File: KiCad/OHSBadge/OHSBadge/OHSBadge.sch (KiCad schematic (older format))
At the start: 100 parts, among them J4 ZIF-40-0.5, P1 PCB, P2 ISP, P3 FTDI, P4 C3SB, P5 JST_3V7, P6 V_IN, P7 UUSB_B, Q1 DMG2301U-7, Q2 2N7002KW, Q3 BSS84W, Q4 2N7002KW, Q5 2N7002KW, Q6 2N7002KW, Q7 BSS84W, SW1 UP, SW2 SEL, SW3 DOWN, SW4 RST, SW5 MODE, U1 MCP9700AT-E/TT, U2 ATMEGA328-AU-ND, U3 MCP1700T-33, U4 TXS0108, U5 DS1307, U5/7 I/O, U6 MCP1702T-50, X1 8MHz, X2 32.768kHz

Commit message: BADGEr v3 swap LED and TEMP.
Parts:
- added G5: OSHW, OSHW_logo, symbol PCB
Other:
- note added: "NOTE : S_LINK (SL1) is bridged [ D2 is bypassed ] when powering the Badge\nfrom the Coin Battery.\nWhen using ANY OTHER power source (Lipo on JST, 5V on USB, 12V Barrel\nsocket etc), Unbridge D2 (remove solder from link SL1).\nThe Coin Battery can then be used as power source for RTC.\nIf RTC is not used, REMOVE the Coin Battery."
- note added: "see NOTE"
- moved on the sheet: H5, H6
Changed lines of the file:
@@
-EESchema Schematic File Version 2  date 23-May-13 1:45:22 PM
+EESchema Schematic File Version 2
 LIBS:OHSBadge_sym
 LIBS:OHSBadge-cache
-EELAYER 27 0
+EELAYER 24 0
 EELAYER END
 $Descr A4 11693 8268
@@
 Text Label 6150 6750 0    40   ~ 0
 SPI_SS_3V3
-Text Label 6150 4750 0    40   ~ 0
+Text Label 6150 5450 0    40   ~ 0
 TEMPERATURE
 Text Label 2025 4275 0    30   ~ 0
@@
 Text Label 6150 5350 0    40   ~ 0
 MODE
-Text Label 6150 5450 0    40   ~ 0
+Text Label 6150 4750 0    40   ~ 0
 AD7_3V3
 Text Label 3825 4100 0    40   ~ 0
@@
 L I/O H5
 U 1 1 5170D6BA
-P 2150 7525
-F 0 "H5" V 2225 7475 40  0000 L CNN
-F 1 "I/O" H 2150 7580 30  0001 C CNN
-F 2 "vite_3mm" H 2150 7525 60  0001 C CNN
-F 3 "~" H 2150 7525 60  0000 C CNN
-	1    2150 7525
+P 2550 7525
+F 0 "H5" V 2625 7475 40  0000 L CNN
+F 1 "I/O" H 2550 7580 30  0001 C CNN
+F 2 "vite_3mm" H 2550 7525 60  0001 C CNN
+F 3 "~" H 2550 7525 60  0000 C CNN
+	1    2550 7525
 	0    -1   -1   0
 $EndComp
@@
 L I/O H6
 U 1 1 5170D6F4
-P 2350 7525
-F 0 "H6" V 2425 7475 40  0000 L CNN
-F 1 "I/O" H 2350 7580 30  0001 C CNN
-F 2 "vite_3mm" H 2350 7525 60  0001 C CNN
-F 3 "~" H 2350 7525 60  0000 C CNN
-	1    2350 7525
+P 2750 7525
+F 0 "H6" V 2825 7475 40  0000 L CNN
+F 1 "I/O" H 2750 7580 30  0001 C CNN
+F 2 "vite_3mm" H 2750 7525 60  0001 C CNN
+F 3 "~" H 2750 7525 60  0000 C CNN
+	1    2750 7525
 	0    -1   -1   0
 $EndComp
-NoConn ~ 2350 7675
-NoConn ~ 2150 7675
+NoConn ~ 2750 7675
+NoConn ~ 2550 7675
 $Comp
 L S_LINK SL1
 U 1 1 5170DF18
 P 10750 6150
-F 0 "SL1" H 10850 6100 30  0000 C CNN
-F 1 "S_LINK" H 10900 6150 30  0000 C CNN
+F 0 "SL1" H 10875 6175 30  0000 C CNN
+F 1 "S_LINK" H 10900 6225 30  0000 C CNN
 F 2 "ShortLink" H 10750 6150 60  0001 C CNN
 F 3 "" H 10750 6150 60  0000 C CNN
@@
 Text Label 6150 5850 0    40   ~ 0
 UP
+Text Notes 8325 5275 0    30   ~ 0
+NOTE : S_LINK (SL1) is bridged [ D2 is bypassed ] when powering the Badge\nfrom the Coin Battery.\nWhen using ANY OTHER power source (Lipo on JST, 5V on USB, 12V Barrel\nsocket etc), Unbridge D2 (remove solder from link SL1).\nThe Coin Battery can then be used as power source for RTC.\nIf RTC is not used,  REMOVE the Coin Battery.
+Text Notes 10825 6200 0    30   ~ 0
+see NOTE
+Wire Notes Line
+	8300 5200 10150 5200
+Wire Notes Line
+	10150 5200 10150 5550
+Wire Notes Line
+	10150 5550 8300 5550
+Wire Notes Line
+	8300 5550 8300 5200
+$Comp
+L PCB G5
+U 1 1 51AE0BF3
+P 2200 7600
+F 0 "G5" H 2200 7550 40  0000 C CNN
+F 1 "OSHW" H 2200 7650 40  0000 C CNN
+F 2 "OSHW_logo" H 2200 7600 60  0001 C CNN
+F 3 "" H 2200 7600 60  0000 C CNN
+	1    2200 7600
+	1    0    0    -1
+$EndComp
 $EndSCHEMATC

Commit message: OHSBadge : BADGEr_v3 Final Prototype. Added PDF Files. Minor mods.
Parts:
- D3: footprint (none) -> led_0805
- G5: footprint OSHW_logo -> OHS2013
- J4: footprint ZIF-40-0.5-M_Hirose -> ZIF-40-0.5-M_seeed
- SD1: footprint SD_Micro -> SD_Micro_seeed
- U4: footprint SO20L -> TXS0108EPWR
- renumbered AD7 to A0, AD7_3V3 to A0_3V3, A3 to XA3, B3 to XB3
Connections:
- net labels added: A0, A0_3V3
- net labels removed: AD7, AD7_3V3
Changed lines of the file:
@@
-EESchema Schematic File Version 2
+EESchema Schematic File Version 2  date 05-Jun-13 3:48:10 PM
 LIBS:OHSBadge_sym
 LIBS:OHSBadge-cache
-EELAYER 24 0
+EELAYER 27 0
 EELAYER END
 $Descr A4 11693 8268
@@
 Sheet 1 1
 Title ""
-Date "23 may 2013"
+Date "5 jun 2013"
 Rev ""
 Comp ""
@@
 F 0 "J4" H 11075 300 27  0000 L TNN
 F 1 "ZIF-40-0.5" H 10875 -1475 27  0000 L TNN
-F 2 "ZIF-40-0.5-M_Hirose" H 10500 575 27  0001 L TNN
+F 2 "ZIF-40-0.5-M_seeed" H 10500 575 27  0001 L TNN
 F 3 "" H 10450 525 60  0001 C CNN
 	1    10450 525
@@
 F 0 "U4" H 1525 3775 40  0000 C CNN
 F 1 "TXS0108" H 1525 3875 40  0000 C CNN
-F 2 "SO20L" H 1525 4175 60  0001 C CNN
+F 2 "TXS0108EPWR" H 1525 4175 60  0001 C CNN
 F 3 "" H 1525 4175 60  0000 C CNN
 	1    1525 4175
@@
 F 0 "SD1" H 1950 3325 40  0000 C CNN
 F 1 "SD_CARD_MICRO" H 2375 3325 40  0000 C CNN
-F 2 "SD_Micro" H 1800 2875 60  0001 C CNN
+F 2 "SD_Micro_seeed" H 1800 2875 60  0001 C CNN
 F 3 "" H 1800 2875 60  0001 C CNN
 	1    1800 2875
@@
 MODE
 Text Label 6150 4750 0    40   ~ 0
-AD7_3V3
+A0_3V3
 Text Label 3825 4100 0    40   ~ 0
 3V3
@@
 $EndComp
 $Comp
-L I/O AD7_3V3
+L I/O A0_3V3
 U 1 1 5159E685
 P 2175 4075
-F 0 "AD7_3V3" H 2225 4075 40  0000 L CNN
+F 0 "A0_3V3" H 2225 4075 40  0000 L CNN
 F 1 "I/O" H 2175 4020 30  0001 C CNN
 F 2 "I/O" H 2175 4075 60  0001 C CNN
@@
 Text Label 3775 1850 0    40   ~ 0
 GND
-Text Label 3775 1750 0    40   ~ 0
-SH_5V
 Text Label 3775 1450 0    40   ~ 0
 SH_5V
@@
 $EndComp
 Text Label 1925 4075 0    30   ~ 0
-AD7_3V3
+A0_3V3
 Text Label 2025 3975 0    30   ~ 0
 SPI_SS_3V3
 Text Label 925  4075 0    30   ~ 0
-AD7
+A0
 Text Label 925  3975 0    30   ~ 0
 SPI_SS
 $Comp
-L I/O AD7
+L I/O A0
 U 1 1 51627367
 P 775 4075
-F 0 "AD7" H 825 4075 40  0000 L CNN
+F 0 "A0" H 825 4075 40  0000 L CNN
 F 1 "I/O" H 775 4020 30  0001 C CNN
 F 2 "I/O" H 775 4075 60  0001 C CNN
@@
 $EndComp
 $Comp
-L I/O B3
+L I/O XB3
 U 1 1 5162736D
 P 775 4175
-F 0 "B3" H 855 4175 40  0000 L CNN
+F 0 "XB3" H 825 4175 40  0000 L CNN
 F 1 "I/O" H 775 4120 30  0001 C CNN
 F 2 "I/O" H 775 4175 60  0001 C CNN
@@
 	3775 1850 4025 1850
 Wire Wire Line
-	3775 1750 4025 1750
-Wire Wire Line
-	3575 1450 4025 1450
-Wire Wire Line
 	8425 6475 8425 6575
 Connection ~ 8425 6000
@@
 Connection ~ 6775 5350
 $Comp
-L I/O A3
+L I/O XA3
 U 1 1 51645932
 P 2175 4175
-F 0 "A3" H 2255 4175 40  0000 L CNN
+F 0 "XA3" H 2225 4175 40  0000 L CNN
 F 1 "I/O" H 2175 4120 30  0001 C CNN
 F 2 "I/O" H 2175 4175 60  0001 C CNN
@@
 Text Label 7950 6000 0    30   ~ 0
 V_IN
-$Comp
-L PWR_FLAG #FLG027
-U 1 1 51669725
-P 3575 1400
-F 0 "#FLG027" H 3575 1305 30  0001 C CNN
-F 1 "PWR_FLAG" V 3475 1500 30  0000 C CNN
-F 2 "" H 3575 1400 60  0000 C CNN
-F 3 "" H 3575 1400 60  0000 C CNN
-	1    3575 1400
-	1    0    0    -1
-$EndComp
-Wire Wire Line
-	3575 1450 3575 1400
 $Comp
 L UUSB_B P7
@@
 	2575 4925 2575 4075
 $Comp
-L PWR_FLAG #FLG028
+L PWR_FLAG #FLG027
 U 1 1 516131E6
 P 10900 5925
-F 0 "#FLG028" H 10900 5830 30  0001 C CNN
+F 0 "#FLG027" H 10900 5830 30  0001 C CNN
 F 1 "PWR_FLAG" H 10900 6100 30  0000 C CNN
 F 2 "" H 10900 5925 60  0000 C CNN
@@
 F 0 "D3" V 10925 4950 30  0000 C CNN
 F 1 "DEBUG" V 10875 5000 30  0000 C CNN
-F 2 "" H 10925 5175 60  0000 C CNN
+F 2 "led_0805" H 10925 5175 60  0001 C CNN
 F 3 "~" H 10925 5175 60  0000 C CNN
 	1    10925 5175
@@
 	10925 5375 10925 5475
 $Comp
-L GND #PWR029
+L GND #PWR028
 U 1 1 519C90C8
 P 10925 5475
-F 0 "#PWR029" H 10925 5475 30  0001 C CNN
+F 0 "#PWR028" H 10925 5475 30  0001 C CNN
 F 1 "GND" H 10925 5545 30  0001 C CNN
 F 2 "" H 10925 5475 60  0000 C CNN
@@
 	10925 4600 10475 4600
 Text Label 10475 4600 0    40   ~ 0
-AD7_3V3
+A0_3V3
 Wire Notes Line
 	10325 4475 11175 4475
@@
 F 0 "G5" H 2200 7550 40  0000 C CNN
 F 1 "OSHW" H 2200 7650 40  0000 C CNN
-F 2 "OSHW_logo" H 2200 7600 60  0001 C CNN
+F 2 "OHS2013" H 2200 7600 60  0001 C CNN
 F 3 "" H 2200 7600 60  0000 C CNN
 	1    2200 7600
 	1    0    0    -1
 $EndComp
+Wire Wire Line
+	4025 1450 3700 1450
+Wire Wire Line
+	3700 1450 3700 1750
+Wire Wire Line
+	3700 1750 4025 1750
 $EndSCHEMATC

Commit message: OHSBadge : BADGEr_v3 Final Prototype. push buttons changed to SMD. Added SMD ON switch for BATTERY. Centered P-Buttons with EPD.
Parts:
- added SW6: SW_ON, SW_SLIDE_seeed, symbol SW_SLIDE
- SW1, SW2, SW3, SW4, SW5: footprint SW-PB -> SW_SMD
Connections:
- net labels added: BATT
- wire segments 368 -> 372
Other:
- moved on the sheet: D3, R14
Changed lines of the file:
@@
-EESchema Schematic File Version 2  date 05-Jun-13 3:48:10 PM
+EESchema Schematic File Version 2  date 07-Jun-13 5:07:04 PM
 LIBS:OHSBadge_sym
 LIBS:OHSBadge-cache
@@
 Sheet 1 1
 Title ""
-Date "5 jun 2013"
+Date "7 jun 2013"
 Rev ""
 Comp ""
@@
 Text Label 875  1725 0    24   ~ 0
 3V3
-Text Label 10600 6000 0    30   ~ 0
+Text Label 10900 6000 0    30   ~ 0
 3V3
 Text Label 7575 575  0    24   ~ 0
@@
 F 0 "SW1" H 6675 4525 30  0000 C CNN
 F 1 "UP" H 6900 4500 30  0000 C CNN
-F 2 "SW-PB" H 6900 4500 60  0001 C CNN
+F 2 "SW_SMD" H 6900 4500 60  0001 C CNN
 F 3 "~" H 6900 4500 60  0000 C CNN
 	1    6900 4500
@@
 F 0 "SW2" H 6800 4525 30  0000 C CNN
 F 1 "SEL" H 7025 4500 30  0000 C CNN
-F 2 "SW-PB" H 7025 4500 60  0001 C CNN
+F 2 "SW_SMD" H 7025 4500 60  0001 C CNN
 F 3 "~" H 7025 4500 60  0000 C CNN
 	1    7025 4500
@@
 F 0 "SW3" H 6925 4525 30  0000 C CNN
 F 1 "DOWN" H 7150 4500 30  0000 C CNN
-F 2 "SW-PB" H 7150 4500 60  0001 C CNN
+F 2 "SW_SMD" H 7150 4500 60  0001 C CNN
 F 3 "~" H 7150 4500 60  0000 C CNN
 	1    7150 4500
@@
 F 0 "SW4" H 3925 4850 30  0000 C CNN
 F 1 "RST" H 3625 4850 30  0000 C CNN
-F 2 "SW-PB" H 3775 4750 60  0001 C CNN
+F 2 "SW_SMD" H 3775 4750 60  0001 C CNN
 F 3 "~" H 3775 4750 60  0000 C CNN
 	1    3775 4750
@@
 Wire Wire Line
 	3575 1650 4025 1650
-Wire Notes Line
-	11175 5675 11175 7150
 Wire Wire Line
 	3575 1650 3575 1625
@@
 F 0 "SW5" H 6550 4525 30  0000 C CNN
 F 1 "MODE" H 6775 4500 30  0000 C CNN
-F 2 "SW-PB" H 6775 4500 60  0001 C CNN
+F 2 "SW_SMD" H 6775 4500 60  0001 C CNN
 F 3 "~" H 6775 4500 60  0000 C CNN
 	1    6775 4500
@@
 $EndComp
 Wire Wire Line
-	10525 6250 10525 6350
-Wire Wire Line
 	10525 6050 10525 6000
 Connection ~ 10525 6000
-Wire Wire Line
-	10525 6300 10900 6300
-Connection ~ 10525 6300
 Wire Notes Line
 	10250 5875 10250 5675
@@
 L PWR_FLAG #FLG027
 U 1 1 516131E6
-P 10900 5925
-F 0 "#FLG027" H 10900 5830 30  0001 C CNN
-F 1 "PWR_FLAG" H 10900 6100 30  0000 C CNN
-F 2 "" H 10900 5925 60  0000 C CNN
-F 3 "" H 10900 5925 60  0000 C CNN
-	1    10900 5925
-	1    0    0    -1
-$EndComp
-Wire Wire Line
-	10900 6000 10900 5925
+P 10750 5925
+F 0 "#FLG027" H 10750 5830 30  0001 C CNN
+F 1 "PWR_FLAG" H 10750 6100 30  0000 C CNN
+F 2 "" H 10750 5925 60  0000 C CNN
+F 3 "" H 10750 5925 60  0000 C CNN
+	1    10750 5925
+	1    0    0    -1
+$EndComp
 Wire Wire Line
 	7800 2775 7800 2825
@@
 $EndComp
 Wire Wire Line
-	10750 6050 10750 6000
+	10750 5925 10750 6050
 Connection ~ 10750 6000
-Wire Wire Line
-	10750 6275 10750 6300
-Connection ~ 10750 6300
 $Comp
 L LED D3
 U 1 1 519C8C9E
-P 10925 5175
-F 0 "D3" V 10925 4950 30  0000 C CNN
-F 1 "DEBUG" V 10875 5000 30  0000 C CNN
-F 2 "led_0805" H 10925 5175 60  0001 C CNN
-F 3 "~" H 10925 5175 60  0000 C CNN
-	1    10925 5175
+P 9425 5175
+F 0 "D3" V 9425 4950 30  0000 C CNN
+F 1 "DEBUG" V 9375 5000 30  0000 C CNN
+F 2 "led_0805" H 9425 5175 60  0001 C CNN
+F 3 "~" H 9425 5175 60  0000 C CNN
+	1    9425 5175
 	0    1    1    0
 $EndComp
@@
 L R R14
 U 1 1 519C8CAC
-P 10925 4775
-F 0 "R14" H 10975 4775 27  0000 L TNN
-F 1 "1k5" V 10910 4710 27  0000 L TNN
-F 2 "r_0805" H 10975 4825 27  0001 L TNN
-F 3 "" H 10925 4775 60  0001 C CNN
-F 4 "0402/100k/5%" H -4525 -3025 60  0001 C CNN "Field4"
-	1    10925 4775
+P 9425 4775
+F 0 "R14" H 9475 4775 27  0000 L TNN
+F 1 "1k5" V 9410 4710 27  0000 L TNN
+F 2 "r_0805" H 9475 4825 27  0001 L TNN
+F 3 "" H 9425 4775 60  0001 C CNN
+F 4 "0402/100k/5%" H -6025 -3025 60  0001 C CNN "Field4"
+	1    9425 4775
 	-1   0    0    -1
 $EndComp
-Wire Wire Line
-	10925 4900 10925 4975
-Wire Wire Line
-	10925 5375 10925 5475
-$Comp
-L GND #PWR028
-U 1 1 519C90C8
-P 10925 5475
-F 0 "#PWR028" H 10925 5475 30  0001 C CNN
-F 1 "GND" H 10925 5545 30  0001 C CNN
-F 2 "" H 10925 5475 60  0000 C CNN
-F 3 "" H 10925 5475 60  0000 C CNN
-	1    10925 5475
-	1    0    0    -1
-$EndComp
-Wire Wire Line
-	10925 4650 10925 4600
-Wire Wire Line
-	10925 4600 10475 4600
-Text Label 10475 4600 0    40   ~ 0
-A0_3V3
 Wire Notes Line
 	10325 4475 11175 4475
 Wire Notes Line
-	11175 4475 11175 5575
-Wire Notes Line
-	11175 5575 10325 5575
-Wire Notes Line
-	10325 5575 10325 4475
-Text Notes 10350 5550 0    40   ~ 8
-DEBUG LED
+	10325 4475 10325 5675
 Wire Wire Line
 	6025 4950 6150 4950
@@
 Wire Notes Line
 	7075 7150 11175 7150
-Wire Notes Line
-	11175 5675 7075 5675
 Text Label 6150 5950 0    40   ~ 0
 SEL
 Text Label 6150 5850 0    40   ~ 0
 UP
-Text Notes 8325 5275 0    30   ~ 0
+Text Notes 9350 4150 0    30   ~ 0
 NOTE : S_LINK (SL1) is bridged [ D2 is bypassed ] when powering the Badge\nfrom the Coin Battery.\nWhen using ANY OTHER power source (Lipo on JST, 5V on USB, 12V Barrel\nsocket etc), Unbridge D2 (remove solder from link SL1).\nThe Coin Battery can then be used as power source for RTC.\nIf RTC is not used,  REMOVE the Coin Battery.
 Text Notes 10825 6200 0    30   ~ 0
 see NOTE
 Wire Notes Line
-	8300 5200 10150 5200
-Wire Notes Line
-	10150 5200 10150 5550
-Wire Notes Line
-	10150 5550 8300 5550
-Wire Notes Line
-	8300 5550 8300 5200
+	9325 4075 11175 4075
+Wire Notes Line
+	11175 4075 11175 4425
+Wire Notes Line
+	11175 4425 9325 4425
+Wire Notes Line
+	9325 4425 9325 4075
 $Comp
 L PCB G5
@@
 Wire Wire Line
 	3700 1750 4025 1750
+Wire Wire Line
+	9425 4900 9425 4975
+Wire Wire Line
+	9425 5375 9425 5475
+$Comp
+L GND #PWR028
+U 1 1 51B1B0BC
+P 9425 5475
+F 0 "#PWR028" H 9425 5475 30  0001 C CNN
+F 1 "GND" H 9425 5545 30  0001 C CNN
+F 2 "" H 9425 5475 60  0000 C CNN
+F 3 "" H 9425 5475 60  0000 C CNN
+	1    9425 5475
+	1    0    0    -1
+$EndComp
+Wire Wire Line
+	9425 4650 9425 4600
+Wire Wire Line
+	9425 4600 8975 4600
+Text Label 8975 4600 0    40   ~ 0
+A0_3V3
+Wire Notes Line
+	8825 4475 9675 4475
+Wire Notes Line
+	9675 4475 9675 5575
+Wire Notes Line
+	9675 5575 8825 5575
+Wire Notes Line
+	8825 5575 8825 4475
+Text Notes 8850 5550 0    40   ~ 8
+DEBUG LED
+Wire Notes Line
+	11175 7150 11175 4475
+Wire Notes Line
+	10325 5675 7075 5675
+$Comp
+L SW_SLIDE SW6
+U 1 1 51B1B845
+P 10900 5325
+F 0 "SW6" H 11140 5375 30  0000 C CNN
+F 1 "SW_ON" H 10900 5245 30  0000 C CNN
+F 2 "SW_SLIDE_seeed" H 10900 5325 60  0001 C CNN
+F 3 "~" H 10900 5325 60  0000 C CNN
+	1    10900 5325
+	0    -1   -1   0
+$EndComp
+Wire Wire Line
+	10900 5025 10900 4800
+Wire Wire Line
+	10525 6250 10525 6300
+Wire Wire Line
+	10525 6300 10900 6300
+Wire Wire Line
+	10750 6275 10750 6300
+Connection ~ 10750 6300
+Wire Wire Line
+	10525 6350 10900 6350
+Wire Wire Line
+	10900 5625 10900 5700
+Wire Wire Line
+	10900 5700 10975 5700
+Wire Wire Line
+	10900 4800 10975 4800
+Text Label 10975 4800 0    30   ~ 0
+BATT_3V
+Text Label 10900 6350 0    30   ~ 0
+BATT
+Text Label 10975 5700 0    30   ~ 0
+BATT
 $EndSCHEMATC

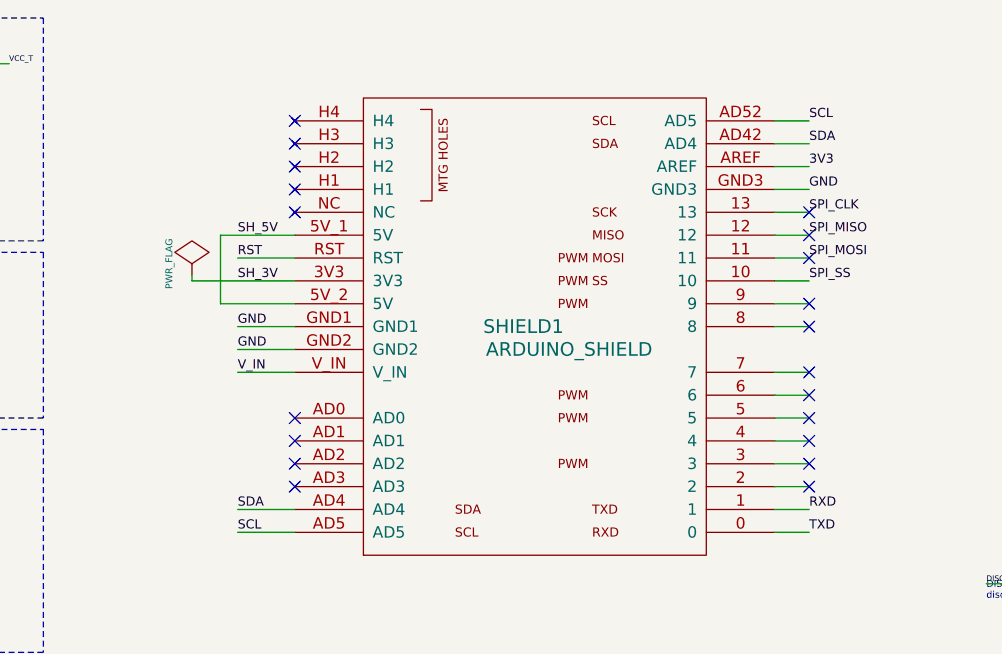
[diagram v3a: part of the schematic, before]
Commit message: OHSBadge : BADGEr_v4 Schematic. Removed 3V3 connection to Arduino shield AREF. Connected Shield 5V0 to VCC of BADGEr
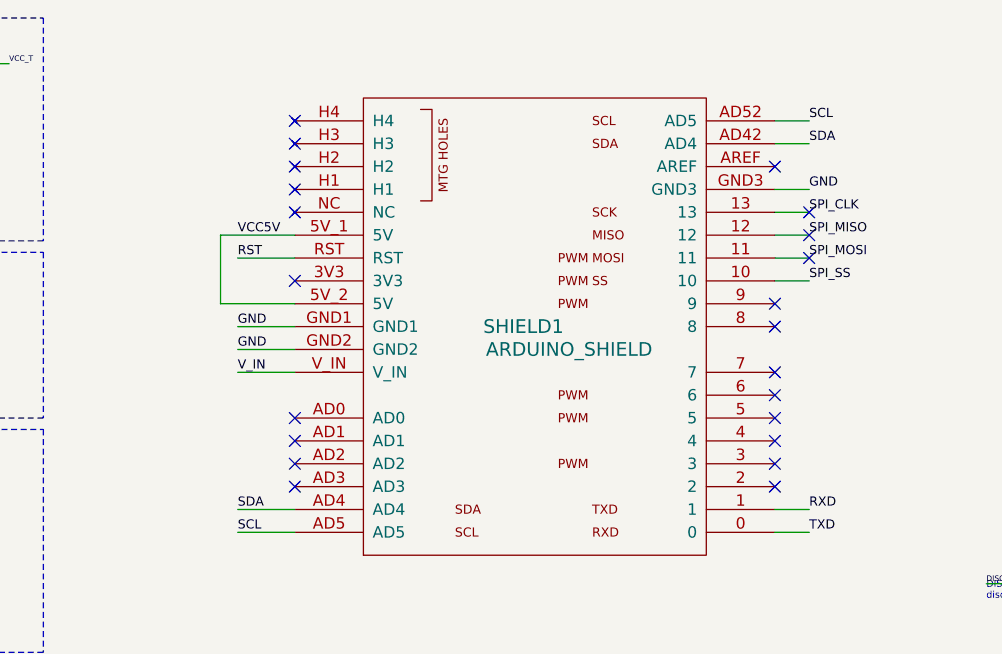
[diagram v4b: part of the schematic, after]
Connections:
- net labels removed: SH_3V, SH_5V
- wire segments 372 -> 361
- no-connect marks 32 -> 34
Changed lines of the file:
@@
-EESchema Schematic File Version 2  date 07-Jun-13 5:07:04 PM
+EESchema Schematic File Version 2  date 11-Jun-13 3:34:23 PM
 LIBS:OHSBadge_sym
 LIBS:OHSBadge-cache
@@
 Sheet 1 1
 Title ""
-Date "7 jun 2013"
+Date "11 jun 2013"
 Rev ""
 Comp ""
@@
 	-1   0    0    -1
 $EndComp
-Text Label 6275 1150 0    40   ~ 0
-3V3
 $Comp
 L SW_PUSH SW1
@@
 Text Notes 700  7300 0    40   ~ 8
 Interfaces_Communication
-NoConn ~ 6275 1750
-NoConn ~ 6275 1850
-NoConn ~ 6275 2550
-NoConn ~ 6275 2450
-NoConn ~ 6275 2350
-NoConn ~ 6275 2250
-NoConn ~ 6275 2150
-NoConn ~ 6275 2050
+NoConn ~ 6125 1750
+NoConn ~ 6125 1850
+NoConn ~ 6125 2550
+NoConn ~ 6125 2450
+NoConn ~ 6125 2350
+NoConn ~ 6125 2250
+NoConn ~ 6125 2150
+NoConn ~ 6125 2050
 Text Label 3775 1950 0    40   ~ 0
 GND
 Text Label 3775 1850 0    40   ~ 0
 GND
-Text Label 3775 1450 0    40   ~ 0
-SH_5V
 Text Label 3775 2650 0    40   ~ 0
 SDA
@@
 Text Label 6275 1650 0    40   ~ 0
 SPI_SS
-Text Label 3775 1650 0    40   ~ 0
-SH_3V
 $Comp
 L BATT_HOLDER BT1
@@
 	0    1    1    0
 $EndComp
-$Comp
-L PWR_FLAG #FLG025
-U 1 1 5161337E
-P 3575 1625
-F 0 "#FLG025" H 3575 1530 30  0001 C CNN
-F 1 "PWR_FLAG" V 3475 1675 30  0000 C CNN
-F 2 "" H 3575 1625 60  0000 C CNN
-F 3 "" H 3575 1625 60  0000 C CNN
-	1    3575 1625
-	1    0    0    -1
-$EndComp
 Text Label 1925 4075 0    30   ~ 0
 A0_3V3
@@
 	10250 2525 10250 3275
 Wire Wire Line
-	6125 2550 6275 2550
-Wire Wire Line
-	6125 2350 6275 2350
-Wire Wire Line
-	6125 2150 6275 2150
-Wire Wire Line
-	6125 1850 6275 1850
-Wire Wire Line
 	6125 1450 6275 1450
 Wire Wire Line
@@
 Wire Wire Line
 	6125 1550 6275 1550
-Wire Wire Line
-	6125 1750 6275 1750
-Wire Wire Line
-	6125 2050 6275 2050
-Wire Wire Line
-	6125 2250 6275 2250
-Wire Wire Line
-	6125 2450 6275 2450
-Wire Wire Line
-	6275 1150 6125 1150
 Wire Wire Line
 	2150 3450 2150 3500
@@
 	3750 5150 3450 5150
 Connection ~ 3450 5150
-Wire Wire Line
-	3575 1650 4025 1650
-Wire Wire Line
-	3575 1650 3575 1625
 Wire Wire Line
 	3775 1550 4025 1550
@@
 3V3
 $Comp
-L GND #PWR026
+L GND #PWR025
 U 1 1 51642116
 P 1325 6175
-F 0 "#PWR026" H 1325 6175 30  0001 C CNN
+F 0 "#PWR025" H 1325 6175 30  0001 C CNN
 F 1 "GND" H 1325 6105 30  0001 C CNN
 F 2 "" H 1325 6175 60  0001 C CNN
@@
 	2575 4925 2575 4075
 $Comp
-L PWR_FLAG #FLG027
+L PWR_FLAG #FLG026
 U 1 1 516131E6
 P 10750 5925
-F 0 "#FLG027" H 10750 5830 30  0001 C CNN
+F 0 "#FLG026" H 10750 5830 30  0001 C CNN
 F 1 "PWR_FLAG" H 10750 6100 30  0000 C CNN
 F 2 "" H 10750 5925 60  0000 C CNN
@@
 	9425 5375 9425 5475
 $Comp
-L GND #PWR028
+L GND #PWR027
 U 1 1 51B1B0BC
 P 9425 5475
-F 0 "#PWR028" H 9425 5475 30  0001 C CNN
+F 0 "#PWR027" H 9425 5475 30  0001 C CNN
 F 1 "GND" H 9425 5545 30  0001 C CNN
 F 2 "" H 9425 5475 60  0000 C CNN
@@
 Text Label 10975 5700 0    30   ~ 0
 BATT
+Text Label 3775 1450 0    40   ~ 0
+VCC5V
+NoConn ~ 4025 1650
+NoConn ~ 6125 1150
 $EndSCHEMATC

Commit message: OHSBadge : BADGEr_v4. Disconnect V_IN between Shield and Badge
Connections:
- wire segments 361 -> 360
- no-connect marks 34 -> 35
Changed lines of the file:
@@
-EESchema Schematic File Version 2  date 11-Jun-13 3:34:23 PM
+EESchema Schematic File Version 2  date 11-Jun-13 4:01:15 PM
 LIBS:OHSBadge_sym
 LIBS:OHSBadge-cache
@@
 encoding utf-8
 Sheet 1 1
-Title ""
+Title "BADGEr_v4"
 Date "11 jun 2013"
 Rev ""
@@
 	9225 6625 9225 6000
 Connection ~ 9225 6000
-Wire Wire Line
-	3775 2050 4025 2050
-Text Label 3775 2050 0    40   ~ 0
-V_IN
 Text Label 10900 6300 0    30   ~ 0
 BATT_3V
@@
 NoConn ~ 4025 1650
 NoConn ~ 6125 1150
+NoConn ~ 4025 2050
 $EndSCHEMATC

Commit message: OHSBadge : BADGEr_v4. Added DNP to unpopulated parts on schematic. Max. Page turns BATT warning on Back Legend. Breakout Pads for unused Shield headers
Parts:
- added AD0, AD1, AD2, AD3, AREF1, PD11, PD12, PD13, PD2, PD4, PD5, PD6, PD7, PD8, PD9, V1, V2: I/O, I/O, symbol I/O
- P2, P4, P5, P7, U5: Field4 (none) -> DNP
- P6: Field12 (none) -> DNP
- X2: Field5 (none) -> DNP
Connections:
- net labels added: 3V, AD0, AD1, AD2, AD3, PD11, PD12, PD13, PD2, PD4, PD5, PD6, PD7, PD8, PD9, VIN
- net labels removed: SPI_CLK, SPI_MISO, SPI_MOSI
- wire segments 360 -> 375
- no-connect marks 35 -> 18
